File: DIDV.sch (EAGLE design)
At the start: 197 parts, among them IC1 PIC18F4550_TQFP

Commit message: -  Inclusão do circuito de buzzer; -  Correção e prevenção contra ruídos nas linhas comunicação;
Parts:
- removed C1, C2: (no value), rcl:C-EUC0805
- removed D1: BAS40, diode:BAS40
- removed JP1: (no value), jumper:JP1Q
- removed Q1: (no value), crystal:CRYSTALHC49UP
- removed R1, R2: (no value), rcl:R-EU_R0603
- added C30, C31, C32, C33, C34, C35, C36, C37, C38, C39, C40, C41, C42, C43, C44, C46: (no value), rcl:C-EUC0603K
- added C45: (no value), rcl:C-USC0805K
- added D5: BAS40, diode:BAS40
- added D6: BAS21, diode:BAS40
- added JP4: (no value), jumper:JP2E
- added LSP1: LSP10, solpad:LSP10
- added Q3: (no value), crystal:CRYSTALHC49U-V
- added Q4: BC817, transistor-npn:BC817-16LT1SMD
- added R105, R106, R107, R108, R109, R110, R111, R112, R113: (no value), rcl:R-EU_R0603
- added SG2: F/CM12P, buzzer:F/CM12P
- added SJ6: JUMPER-PAD-3-2OF3_NC_BY_PASTE, SparkFun-Passives:JUMPER-PAD-3-2OF3_NC_BY_PASTE
- C15, C16, C4: device rcl:C-EUC0603K -> rcl:C-EUC0805
- C3: device rcl:CPOL-EU140CLH-1014 -> rcl:C-EUC0805
- C5: device rcl:C-EUC0805 -> rcl:CPOL-EU140CLH-1014
- C6: device rcl:C-EUC0805 -> rcl:C-EUC0603K
- D2: value (none) -> BAS40; device diode:DIODE-SMC -> diode:BAS40
- D3: value BAS70 -> (none); device diode:BAS70 -> diode:DIODE-SMC
- D4: value BAS40 -> BAS70; device diode:BAS40 -> diode:BAS70
- JP2: device jumper:JP1E -> jumper:JP1Q
- JP3: device jumper:JP2E -> jumper:JP1E
- Q2: device crystal:CRYSTALHC49U-V -> crystal:CRYSTALHC49UP
- R5, R6: device rcl:R-US_R0805 -> rcl:R-EU_R0603
- R77, R78: device rcl:R-EU_R0603 -> rcl:R-US_R0805
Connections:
- removed net N$3: R81.2, S3.1, S3.2
- removed net N$43: IC1.RA2/AN2/VREF-/CVREF
- removed net N$9: C5.1, C6.1, D4.C, L1.1
- new net BUZZER: IC1.RB3/AN9/CCP2/VPO, SJ6.1
- new net N$10: C34.2, IC4.SIN, R109.2
- new net N$12: C35.2, IC5.SIN, R110.2
- new net N$13: IC5.SOUT, R111.1
- new net N$17: LSP1.MP, SJ6.3
- new net N$2: C7.1, C8.1, D5.C, L1.1
- new net N$23: C45.2, D6.A, Q4.C, SG2.1
- new net N$24: R112.1, SJ6.2
- new net N$25: C46.1, Q4.B, R112.2, R113.2
- new net N$5: R85.2, S3.1, S3.2
- new net N$6: C32.2, IC2.SIN, R107.2
- new net N$7: C33.2, IC3.SIN, R108.2
- net AGND: now also C3.2, C30.2, C31.2, C32.1, C33.1, C34.1, C35.1, C36.2, C37.2, C38.2, C39.2, C40.2, C41.2, C42.2, C43.2, C44.1, C46.2, C5.-, D4.A, JP2.1, JP4.1, Q4.E, R105.1, R113.1, R23.1, R3.1, R40.1, R57.1, R97.1, R98.1; no longer C1.2, C2.2, C3.-, C5.2, D3.A, JP1.1, JP3.1, R1.1, R103.1, R21.1, R38.1, R55.1, R72.1, R73.1
- net B00: now also C19.1; no longer C17.1
- net B01: now also C20.1; no longer C18.1
- net B02: now also C21.1; no longer C19.1
- net B03: now also C22.1; no longer C20.1
- net B04: now also C23.1; no longer C21.1
- net B05: now also C30.1; no longer C28.1
- net BACKSPACE: now also C25.1, R100.1; no longer C23.1, R98.1
- net D+: now also R6.1; no longer R4.1
- net D-: now also R5.1; no longer R3.1
- net DOWN: now also C31.1, R106.1; no longer C29.1, R104.1
- net ENTER: now also C24.1, R99.1; no longer C22.1, R97.1
- net ESC: now also C26.1, R101.1; no longer C24.1, R99.1
- net ESPAÇO: now also C27.1, R102.1; no longer C25.1, R100.1
- net FIM: now also C28.1, IC1.RA2/AN2/VREF-/CVREF, R103.1; no longer C26.1, IC1.RB3/AN9/CCP2/VPO, R101.1
- net GSCLK: now also C36.1, C37.1, C38.1, C39.1
- net M00: now also R58.1; no longer R56.1
- net M01: now also R59.1; no longer R57.1
- net M02: now also R60.1; no longer R58.1
- net M03: now also R61.1; no longer R59.1
- net M04: now also R62.1; no longer R60.1
- net M05: now also R63.1; no longer R61.1
- net M06: now also R64.1; no longer R62.1
- net M07: now also R65.1; no longer R63.1
- net M08: now also R66.1; no longer R64.1
- net M09: now also R67.1; no longer R65.1
- net M10: now also R68.1; no longer R66.1
- net M11: now also R69.1; no longer R67.1
- net M12: now also R70.1; no longer R68.1
- net M13: now also R71.1; no longer R69.1
- net M14: now also R72.1; no longer R70.1
- net M15: now also R73.1; no longer R71.1
- net M16: now also R7.1; no longer R5.1
- net M17: now also R8.1; no longer R6.1
- net M18: now also R9.1; no longer R7.1
- net M19: now also R10.1; no longer R8.1
- net M20: now also R11.1; no longer R9.1
- net M21: now also R12.1; no longer R10.1
- net M22: now also R13.1; no longer R11.1
- net M23: now also R14.1; no longer R12.1
- net M24: now also R15.1; no longer R13.1
- net M25: now also R16.1; no longer R14.1
- net M26: now also R17.1; no longer R15.1
- net M27: now also R18.1; no longer R16.1
- net M28: now also R19.1; no longer R17.1
- net M29: now also R20.1; no longer R18.1
- net M30: now also R21.1; no longer R19.1
- net M31: now also R22.1; no longer R20.1
- net M32: now also R41.1; no longer R39.1
- net M33: now also R42.1; no longer R40.1
- net M34: now also R43.1; no longer R41.1
- net M35: now also R44.1; no longer R42.1
- net M36: now also R45.1; no longer R43.1
- net M37: now also R46.1; no longer R44.1
- net M38: now also R47.1; no longer R45.1
- net M39: now also R48.1; no longer R46.1
- net M40: now also R49.1; no longer R47.1
- net M41: now also R50.1; no longer R48.1
- net M42: now also R51.1; no longer R49.1
- net M43: now also R52.1; no longer R50.1
- net M44: now also R53.1; no longer R51.1
- net M45: now also R54.1; no longer R52.1
- net M46: now also R55.1; no longer R53.1
- net M47: now also R56.1; no longer R54.1
- net M48: now also R24.1; no longer R22.1
- net M49: now also R25.1; no longer R23.1
- net M50: now also R26.1; no longer R24.1
- net M51: now also R27.1; no longer R25.1
- net M52: now also R28.1; no longer R26.1
- net M53: now also R29.1; no longer R27.1
- net M54: now also R30.1; no longer R28.1
- net M55: now also R31.1; no longer R29.1
- net M56: now also R32.1; no longer R30.1
- net M57: now also R33.1; no longer R31.1
- net M58: now also R34.1; no longer R32.1
- net M59: now also R35.1; no longer R33.1
- net M60: now also R36.1; no longer R34.1
- net M61: now also R37.1; no longer R35.1
- net M62: now also R38.1; no longer R36.1
- net M63: now also R39.1; no longer R37.1
- net MCLR: now also JP3.1; no longer JP2.1
- net N$109: now also D3.A, JP2.2; no longer D2.A, JP1.2
- net N$110: now also R3.2; no longer R1.2
- net N$111: now also C6.1, D2.C; no longer C4.1, D1.C
- net N$112: now also D2.A, R4.1; no longer D1.A, R2.1
- net N$113: now also C3.1, C4.1, C5.+, D4.C; no longer C1.1, C2.1, C3.+, D2.C
- net N$114: now also D5.A; no longer D4.A
- net N$115: now also R6.2; no longer R4.2
- net N$116: now also R5.2; no longer R3.2
- net N$118: now also R57.2, R77.2; no longer R55.2, R75.2
- net N$14: now also R79.2; no longer R77.2
- net N$144: now also R74.2, R75.2; no longer R72.2, R73.2
- net N$31: now also R82.2; no longer R80.2
- net N$38: now also R81.2; no longer R79.2
- net N$39: now also R80.2; no longer R78.2
- net N$64: now also R23.2, R76.2; no longer R21.2, R74.2
- net N$68: now also R98.2; no longer R88.2
- net N$69: now also R97.2; no longer R87.2
- net N$70: now also R88.2; no longer R86.2
- net N$71: now also R87.2; no longer R85.2
- net N$72: now also R86.2; no longer R82.2
- net N$8: now also R105.2; no longer R103.2
- net N$85: now also R40.2, R78.2; no longer R38.2, R76.2
- net OSC1: now also C17.1, Q3.1; no longer C15.1, Q1.1
- net OSC2: now also C18.1, Q3.2; no longer C16.1, Q1.2
- net PGC_OUT: now also JP4.3; no longer JP3.3
- net PGD_OUT: now also JP4.2; no longer JP3.2
- net SCLK: now also C40.1, C41.1, C42.1, C43.1
- net SIN: now also R107.1; no longer IC2.SIN
- net SO2: now also R108.1; no longer IC3.SIN
- net SO3: now also R109.1; no longer IC4.SIN
- net SO4: now also R110.1; no longer IC5.SIN
- net SOUT: now also C44.2, R111.2; no longer IC5.SOUT
- net UP: now also C29.1, R104.1; no longer C27.1, R102.1
- net VCC: now also C15.1, C16.1, C45.1, D6.C, JP3.2, R103.2, R106.2, R21.2, R38.2, R4.2, R55.2, R72.2, R73.2, SG2.2; no longer C10.1, C9.1, JP2.2, R2.2, R23.2, R40.2, R5.2, R57.2, R6.2, R97.2, R98.2
- net VUSB: now also C10.1, C9.1; no longer C7.1, C8.1
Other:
- note added: "On Raspberry Pi B+"
- moved on the sheet: C10, C11, C12, C13, C14, C15, C16, C17, C18, C19, C20, C21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

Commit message: Rev4 - Adição do circuito de Alta Latência - Previsão de conexão de módulos de expansão - Correção de falhas e previsão de melhorias com relação a estabilidade do sistema - Definição dos valores iniciais para cada componente - Previsão de circuito conversor de nivel para possivel feature implementável de atualização de firmware.
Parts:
- removed C10, C11, C12, C13, C14, C15, C16, C3, C4, C7, C8, C9: (no value), rcl:C-EUC0805
- removed C17, C18, C19, C20, C21, C22, C23, C24, C25, C31, C6: (no value), rcl:C-EUC0603K
- removed C5: (no value), rcl:CPOL-EU140CLH-1014
- removed D2, D5: BAS40, diode:BAS40
- removed D3: (no value), diode:DIODE-SMC
- removed JP2: (no value), jumper:JP1Q
- removed JP3: (no value), jumper:JP1E
- removed JP4: (no value), jumper:JP2E
- removed L1: (no value), inductor-neosid:MS50
- removed LSP1: LSP10, solpad:LSP10
- removed Q2: (no value), crystal:CRYSTALHC49UP
- removed Q3: (no value), crystal:CRYSTALHC49U-V
- removed Q4: BC817, transistor-npn:BC817-16LT1SMD
- removed R10, R11, R12, R13, R14, R15, R16, R17, R18, R19, R20, R21, R22, R23, R24, R25, R26, R27, R28, R29, R30, R31, R32, R33, R34, R35, R36, R37, R38, R39, R40, R41, R42, R43, R44, R49, R7, R8, R9: (no value), rcl:R-US_R0805
- removed R3, R4, R5, R6: (no value), rcl:R-EU_R0603
- removed S1, S10, S11, S12, S13, S2, S3, S4, S5, S6, S7, S8, S9: (no value), SparkFun-Electromechanical:TAC_SWITCHSMD
- removed SG2: F/CM12P, buzzer:F/CM12P
- removed SJ6: JUMPER-PAD-3-2OF3_NC_BY_PASTE, SparkFun-Passives:JUMPER-PAD-3-2OF3_NC_BY_PASTE
- added C47, C56: 10nf/50V, rcl:C-EUC0603K
- added C48, C49, C50, C51, C52, C53, C54, C55: 100nf/50V, rcl:C-EUC0805
- added D7, D8: BAS21, diode:BAS40
- added JP75, JP86: (no value), jumper:JP1Q
- added JP83: (no value), jumper:JP2E
- added JP84: (no value), jumper:JP1E
- added JP85: (no value), jumper:JP7Q
- added K1: 4052, relay:4052
- added L3: 330m, inductor-neosid:MS50
- added Q10: BC817, transistor-npn:BC817-16LT1SMD
- added R114, R115, R116, R117, R118, R119, R120, R122, R124: (no value), rcl:R-US_R0805
- added R121, R123: 649, rcl:R-US_R0805
- added R125: 22, rcl:R-EU_R0603
- added R126: 10k, rcl:R-EU_R0603
- added R127, R128: 100, rcl:R-EU_R0603
- added R129: 100k, rcl:R-US_R0805
- added R130: 0r, rcl:R-EU_R0603
- added R131: 150k, rcl:R-EU_R0603
- added R132: 100k, rcl:R-EU_R0603
- added XT1: 20Mhz, crystal:CRYSTALHC49UP
- added XT2: (no value), crystal:CRYSTALHC49U-V
- added Z2: 5v1, diode:BAS70
- C26: value (none) -> 470uf/35V; device rcl:C-EUC0603K -> rcl:CPOL-EU140CLH-1014
- C27, C28, C32, C33: value (none) -> 100nf/50V; device rcl:C-EUC0603K -> rcl:C-EUC0805
- C29, C30, C36, C37, C38, C39, C40, C41, C42, C43, C44, C46: value (none) -> 100nf/50V
- C34, C35: value (none) -> 22pf/50V
- C45: value (none) -> 100nf/50V; device rcl:C-USC0805K -> rcl:C-EUC0603K
- D4: value BAS70 -> S3J; device diode:BAS70 -> diode:DIODE-SMC
- IC1: value PIC18F4550_TQFP -> (none); device microchip:PIC18F4550_TQFP -> TLC5940:IC-PACKAGE_DIL28-3
- IC5: value (none) -> PIC18F4550; device TLC5940:IC-PACKAGE_DIL28-3 -> microchip:PIC18F4550_TQFP
- L2: value (none) -> 330m
- R100, R102, R103, R104, R105, R106, R107, R108, R109, R110, R111, R112, R113, R79, R80, R81, R83, R85, R87, R88, R89, R90, R91, R92, R93, R94, R95, R96, R97, R98: device rcl:R-EU_R0603 -> rcl:R-US_R0805
- R101, R99: value (none) -> 22
- R58, R60, R70, R77: value (none) -> 22; device rcl:R-US_R0805 -> rcl:R-EU_R0603
- R82, R84: value (none) -> 649; device rcl:R-EU_R0603 -> rcl:R-US_R0805
- R86: value (none) -> 1M
- SJ1: value JUMPER-PAD-2-NOYES_SILK -> JUMPER-PAD-3-2OF3_NC_BY_PASTE; device SparkFun-Passives:JUMPER-PAD-2-NOYES_SILK -> SparkFun-Passives:JUMPER-PAD-3-2OF3_NC_BY_PASTE
- SJ3: value JUMPER-PAD-3-2OF3_NC_BY_PASTE -> JUMPER-PAD-2-NOYES_SILK; device SparkFun-Passives:JUMPER-PAD-3-2OF3_NC_BY_PASTE -> SparkFun-Passives:JUMPER-PAD-2-NOYES_SILK
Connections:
- removed net B00: C19.1, IC1.RD0/SPP0, R91.1, S9.3, S9.4
- removed net B01: C20.1, IC1.RD1/SPP1, R92.1, S10.3, S10.4
- removed net B02: C21.1, IC1.RD2/SPP2, R93.1, S11.3, S11.4
- removed net B03: C22.1, IC1.RD3/SPP3, R94.1, S12.3, S12.4
- removed net B04: C23.1, IC1.RD4/SPP4, R95.1, S8.3, S8.4
- removed net B05: C30.1, IC1.RD5/SPP5/P1B, R96.1, S7.3, S7.4
- removed net BACKSPACE: C25.1, IC1.RC1/T1OSI/ICCP2/!UOE, R100.1, S4.3, S4.4
- removed net BUZZER: IC1.RB3/AN9/CCP2/VPO, SJ6.1
- removed net DOWN: C31.1, IC1.RD7/SPP7/P1D, R106.1, S14.3, S14.4
- removed net ENTER: C24.1, IC1.RC0/TIOSO/T13CKI, R99.1, S3.3, S3.4
- removed net ESC: C26.1, IC1.RB2/AN8/INT2/VMO, R101.1, S5.3, S5.4
- removed net ESPAÇO: C27.1, IC1.RC6/TX/CK, R102.1, S6.3, S6.4
- removed net FIM: C28.1, IC1.RA2/AN2/VREF-/CVREF, R103.1, S2.3, S2.4
- removed net N$10: C34.2, IC4.SIN, R109.2
- removed net N$109: D3.A, JP2.2
- removed net N$110: R3.2, S13.1, S13.2
- removed net N$111: C6.1, D2.C, R89.2, S13.3, S13.4
- removed net N$112: D2.A, R4.1
- removed net N$113: C3.1, C4.1, C5.+, D3.C, D4.C, L2.1
- removed net N$114: D5.A, U1.VBUS
- removed net N$115: R6.2, U1.D+
- removed net N$116: R5.2, U1.D-
- removed net N$118: IC4.IREF, R57.2, R77.2
- removed net N$12: C35.2, IC5.SIN, R110.2
- removed net N$13: IC5.SOUT, R111.1
- removed net N$14: R79.2, S9.1, S9.2
- removed net N$144: IC2.IREF, R74.2, R75.2
- removed net N$17: LSP1.MP, SJ6.3
- removed net N$18: IC1.RE2/AN7/OESPP
- removed net N$19: IC1.RE1/AN6/CK2SPP
- removed net N$2: C7.1, C8.1, D5.C, L1.1
- removed net N$20: IC1.RE0/AN5/CK1SPP
- removed net N$21: IC1.RA5/AN4/!SS!/HLVDIN/C2OUT
- removed net N$22: IC1.RA4/T0CKI/CIOUT/RCV
- removed net N$23: C45.2, D6.A, Q4.C, SG2.1
- removed net N$24: R112.1, SJ6.2
- removed net N$25: C46.1, Q4.B, R112.2, R113.2
- removed net N$29: R84.2, S7.1, S7.2
- removed net N$30: R83.2, S8.1, S8.2
- removed net N$31: R82.2, S12.1, S12.2
- removed net N$36: IC1.RB4/AN11/KBI0/CSSPP
- removed net N$37: IC1.RB5/KBI1/PGM
- removed net N$38: R81.2, S11.1, S11.2
- removed net N$39: R80.2, S10.1, S10.2
- removed net N$44: IC1.RA3/AN3/VREF+
- removed net N$5: R85.2, S3.1, S3.2
- removed net N$6: C32.2, IC2.SIN, R107.2
- removed net N$64: IC3.IREF, R23.2, R76.2
- removed net N$68: R98.2, S1.1, S1.2
- removed net N$69: R97.2, S2.1, S2.2
- removed net N$7: C33.2, IC3.SIN, R108.2
- removed net N$70: R88.2, S6.1, S6.2
- removed net N$71: R87.2, S5.1, S5.2
- removed net N$72: R86.2, S4.1, S4.2
- removed net N$8: R105.2, S14.1, S14.2
- removed net N$85: IC5.IREF, R40.2, R78.2
- removed net UP: C29.1, IC1.RD6/SPP6/P1C, R104.1, S1.3, S1.4
- new net EXP: IC5.RD4/SPP4, R131.2
- new net EXPA: JP85.4, K12.S
- new net EXPB: JP85.3, K13.P
- new net N$126: IC5.RE2/AN7/OESPP
- new net N$127: IC5.RE1/AN6/CK2SPP
- new net N$128: IC5.RE0/AN5/CK1SPP
- new net N$129: IC5.RA5/AN4/!SS!/HLVDIN/C2OUT
- new net N$130: IC5.RA4/T0CKI/CIOUT/RCV
- new net N$131: IC5.RB4/AN11/KBI0/CSSPP
- new net N$132: IC5.RB5/KBI1/PGM
- new net N$133: IC5.RA3/AN3/VREF+
- new net N$134: R127.2, S14.1, S14.2
- new net N$135: C47.1, D7.C, R128.2, S14.3, S14.4
- new net N$136: D7.A, R126.1
- new net N$137: D4.A, JP75.2
- new net N$138: C26.+, C27.1, C28.1, D4.C, L2.1, Z2.C
- new net N$139: R70.2, U1.D+
- new net N$140: R77.2, U1.D-
- new net N$141: D6.A, U1.VBUS
- new net N$142: IC1.IREF, R82.2, R83.2
- new net N$143: IC3.IREF, R121.2, R122.2
- new net N$145: IC4.IREF, R123.2, R124.2
- new net N$146: IC2.IREF, R84.2, R85.2
- new net N$147: C32.1, C33.1, D6.C, L3.1
- new net N$148: C30.2, IC2.SIN, R60.2
- new net N$149: C29.2, IC1.SIN, R58.2
- new net N$150: C37.2, IC4.SIN, R101.2
- new net N$151: C36.2, IC3.SIN, R99.2
- new net N$152: IC3.SOUT, R125.1
- new net N$153: IC5.RC1/T1OSI/ICCP2/!UOE
- new net N$154: IC5.RD0/SPP0
- new net N$155: IC5.RD1/SPP1
- new net N$156: IC5.RD2/SPP2
- new net N$157: IC5.RD3/SPP3
- new net N$158: IC5.RC6/TX/CK
- new net N$159: IC5.RC0/TIOSO/T13CKI
- new net N$160: IC5.RA2/AN2/VREF-/CVREF
- new net N$161: IC5.!MCLR!/VPP/RE3
- new net N$162: IC5.RB2/AN8/INT2/VMO
- new net N$163: IC5.RB3/AN9/CCP2/VPO
- new net N$164: IC5.RD7/SPP7/P1D
- new net N$165: IC5.RD6/SPP6/P1C
- new net N$166: Q10.C, R130.1
- new net N$167: C56.1, Q10.B, R131.1, R132.2
- new net N$168: D8.A, K11.2, R130.2
- new net N$169: K13.O
- new net RA: IC5.RD5/SPP5/P1B, JP85.2, JP86.2, R129.1
- new net RB: JP85.1, JP86.1
- new net SOUT_: IC5.RB0/AN12/INT0/LFT0/SDI/SDA, K12.O, K13.S
- net AGND: now also C26.-, C29.1, C30.1, C32.2, C33.2, C34.2, C35.2, C36.1, C37.1, C38.1, C44.2, C45.2, C47.2, C48.2, C49.2, C50.2, C51.2, C52.2, C53.2, C54.2, C55.2, C56.2, IC1.GND, IC5.VSS, IC5.VSS@1, JP75.1, JP83.1, JP85.11, JP85.13, Q10.E, R121.1, R122.1, R123.1, R124.1, R127.1, R132.1, Z2.A; no longer C10.2, C11.2, C12.2, C13.2, C14.2, C15.2, C16.2, C17.2, C18.2, C19.2, C20.2, C21.2, C22.2, C23.2, C24.2, C25.2, C26.2, C29.2, C3.2, C30.2, C31.2, C32.1, C33.1, C34.1, C35.1, C36.2, C37.2, C38.2, C4.2, C44.1, C5.-, C6.2, C7.2, C8.2, C9.2, D4.A, IC1.VSS, IC1.VSS@1, IC5.GND, JP2.1, JP4.1, Q4.E, R105.1, R113.1, R23.1, R3.1, R40.1, R57.1, R74.1, R75.1, R76.1, R77.1, R78.1, R79.1, R80.1, R81.1, R86.1, R87.1, R88.1, R97.1, R98.1
- net BLANK: now also IC1.BLANK, IC5.RA1/AN1, JP85.7, TP21.1, TP22.1, TP7.1, TP8.1; no longer IC1.RA1/AN1, IC5.BLANK, TP11.1, TP18.1, TP25.1, TP4.1
- net D+: now also R70.1, SJ2.3; no longer R6.1, SJ4.3
- net D+_: now also IC5.RC5/D+/VP, SJ2.2; no longer IC1.RC5/D+/VP, SJ4.2
- net D-: now also R77.1, SJ1.3; no longer R5.1, SJ5.3
- net D-_: now also IC5.RC4/D-/VM, SJ1.2; no longer IC1.RC4/D-/VM, SJ5.2
- net GSCLK: now also C43.1, C44.1, C45.1, C46.1, IC1.GSCLK, IC5.RC2/CCP1/P1A, JP85.5, TP11.1, TP12.1, TP25.1, TP26.1; no longer C36.1, C37.1, C38.1, C39.1, IC1.RC2/CCP1/P1A, IC5.GSCLK, TP13.1, TP20.1, TP27.1, TP6.1
- net M00: now also R46.1; no longer R58.1
- net M01: now also R48.1; no longer R59.1
- net M02: now also R51.1; no longer R60.1
- net M03: now also R53.1; no longer R61.1
- net M04: now also R55.1; no longer R62.1
- net M05: now also R57.1; no longer R63.1
- net M06: now also R61.1; no longer R64.1
- net M07: now also R63.1; no longer R65.1
- net M08: now also R65.1; no longer R66.1
- net M10: now also R69.1; no longer R68.1
- net M11: now also R72.1; no longer R69.1
- net M12: now also R74.1; no longer R70.1
- net M13: now also R76.1; no longer R71.1
- net M14: now also R79.1; no longer R72.1
- net M15: now also R81.1; no longer R73.1
- net M16: now also IC1.OUT0, R45.1; no longer IC3.OUT0, R7.1
- net M17: now also IC1.OUT1, R47.1; no longer IC3.OUT1, R8.1
- net M18: now also IC1.OUT2, R50.1; no longer IC3.OUT2, R9.1
- net M19: now also IC1.OUT3, R52.1; no longer IC3.OUT3, R10.1
- net M20: now also IC1.OUT4, R54.1; no longer IC3.OUT4, R11.1
- net M21: now also IC1.OUT5, R56.1; no longer IC3.OUT5, R12.1
- net M22: now also IC1.OUT6, R59.1; no longer IC3.OUT6, R13.1
- net M23: now also IC1.OUT7, R62.1; no longer IC3.OUT7, R14.1
- net M24: now also IC1.OUT8, R64.1; no longer IC3.OUT8, R15.1
- net M25: now also IC1.OUT9, R66.1; no longer IC3.OUT9, R16.1
- net M26: now also IC1.OUT10, R68.1; no longer IC3.OUT10, R17.1
- net M27: now also IC1.OUT11, R71.1; no longer IC3.OUT11, R18.1
- net M28: now also IC1.OUT12, R73.1; no longer IC3.OUT12, R19.1
- net M29: now also IC1.OUT13, R75.1; no longer IC3.OUT13, R20.1
- net M30: now also IC1.OUT14, R78.1; no longer IC3.OUT14, R21.1
- net M31: now also IC1.OUT15, R80.1; no longer IC3.OUT15, R22.1
- net M32: now also R88.1; no longer R41.1
- net M33: now also R90.1; no longer R42.1
- net M34: now also R92.1; no longer R43.1
- net M35: now also R94.1; no longer R44.1
- net M36: now also R96.1; no longer R45.1
- net M37: now also R98.1; no longer R46.1
- net M38: now also R102.1; no longer R47.1
- net M39: now also R104.1; no longer R48.1
- net M40: now also R106.1; no longer R49.1
- net M41: now also R108.1; no longer R50.1
- net M42: now also R110.1; no longer R51.1
- net M43: now also R112.1; no longer R52.1
- net M44: now also R114.1; no longer R53.1
- net M45: now also R116.1; no longer R54.1
- net M46: now also R118.1; no longer R55.1
- net M47: now also R120.1; no longer R56.1
- net M48: now also IC3.OUT0, R87.1; no longer IC5.OUT0, R24.1
- net M49: now also IC3.OUT1, R89.1; no longer IC5.OUT1, R25.1
- net M50: now also IC3.OUT2, R91.1; no longer IC5.OUT2, R26.1
- net M51: now also IC3.OUT3, R93.1; no longer IC5.OUT3, R27.1
- net M52: now also IC3.OUT4, R95.1; no longer IC5.OUT4, R28.1
- net M53: now also IC3.OUT5, R97.1; no longer IC5.OUT5, R29.1
- net M54: now also IC3.OUT6, R100.1; no longer IC5.OUT6, R30.1
- net M55: now also IC3.OUT7, R103.1; no longer IC5.OUT7, R31.1
- net M56: now also IC3.OUT8, R105.1; no longer IC5.OUT8, R32.1
- net M57: now also IC3.OUT9, R107.1; no longer IC5.OUT9, R33.1
- net M58: now also IC3.OUT10, R109.1; no longer IC5.OUT10, R34.1
- net M59: now also IC3.OUT11, R111.1; no longer IC5.OUT11, R35.1
- net M60: now also IC3.OUT12, R113.1; no longer IC5.OUT12, R36.1
- net M61: now also IC3.OUT13, R115.1; no longer IC5.OUT13, R37.1
- net M62: now also IC3.OUT14, R117.1; no longer IC5.OUT14, R38.1
- net M63: now also IC3.OUT15, R119.1; no longer IC5.OUT15, R39.1
- net MCLR: now also JP84.1, SJ3.1; no longer JP3.1, SJ1.1
- net NC: now also IC1.XERR; no longer IC5.XERR
- net OSC1: now also C34.1, IC5.OSC1/CLKI, R86.2, XT1.1, XT2.1; no longer C17.1, IC1.OSC1/CLKI, Q2.1, Q3.1, R90.2
- net OSC2: now also C35.1, IC5.RA6/OSC2/CLKO, R86.1, XT1.2, XT2.2; no longer C18.1, IC1.RA6/OSC2/CLKO, Q2.2, Q3.2, R90.1
- net PGC: now also IC5.RB6/KBI2/PGC, SJ4.2; no longer IC1.RB6/KBI2/PGC, SJ2.2
- net PGC_OUT: now also JP83.3, SJ4.3; no longer JP4.3, SJ2.3
- net PGD: now also IC5.RB7/BKI3/PGD, SJ5.2; no longer IC1.RB7/BKI3/PGD, SJ3.2
- net PGD_OUT: now also JP83.2, SJ5.3; no longer JP4.2, SJ3.3
- net RB6: now also SJ4.1; no longer SJ2.1
- net RB7: now also SJ5.1; no longer SJ3.1
- net RC4: now also SJ1.1; no longer SJ5.1
- net RC5: now also SJ2.1; no longer SJ4.1
- net RESET: now also R128.1, SJ3.2; no longer IC1.!MCLR!/VPP/RE3, R89.1, SJ1.2
- net SCLK: now also C39.1, IC1.SCLK, IC5.RB1/AN10/INT1/SCK/SCL, JP85.6, TP17.1, TP18.1, TP3.1, TP4.1; no longer C43.1, IC1.RB1/AN10/INT1/SCK/SCL, IC5.SCLK, TP16.1, TP2.1, TP23.1, TP9.1
- net SIN: now also IC5.RC7/RX/DT/SDO, R60.1, TP2.1; no longer IC1.RC7/RX/DT/SDO, R107.1, TP1.1
- net SO2: now also R58.1, TP1.1, TP14.1; no longer R108.1, TP7.1, TP8.1
- net SO3: now also IC1.SOUT, R101.1, TP13.1, TP16.1; no longer IC3.SOUT, R109.1, TP14.1, TP15.1
- net SO4: now also R99.1, TP15.1, TP27.1; no longer R110.1, TP21.1, TP22.1
- net SOUT: now also C38.2, K12.P, R125.2; no longer C44.2, IC1.RB0/AN12/INT0/LFT0/SDI/SDA, R111.2
- net VCC: now also C48.1, C49.1, C50.1, C51.1, C52.1, C53.1, D8.C, IC1.DCPRG, IC1.VCC, IC1.VPRG, IC5.VDD, IC5.VDD@1, JP84.2, JP85.12, JP85.14, K11.1, L3.2, R105.2, R107.2, R108.2, R109.2, R110.2, R111.2, R112.2, R113.2, R114.2, R115.2, R116.2, R117.2, R118.2, R119.2, R120.2, R126.2, R129.2, R57.2, R74.2, R75.2, R76.2, R78.2, R79.2, R80.2, R81.2, R87.2, R88.2, R89.2, R90.2, R97.2, R98.2, TP10.1, TP23.1, TP24.1, TP9.1; no longer C11.1, C12.1, C13.1, C14.1, C15.1, C16.1, C45.1, D6.C, IC1.VDD, IC1.VDD@1, IC5.DCPRG, IC5.VCC, IC5.VPRG, JP3.2, L1.2, R10.2, R101.2, R11.2, R12.2, R13.2, R14.2, R15.2, R16.2, R17.2, R18.2, R19.2, R20.2, R21.2, R22.2, R24.2, R25.2, R26.2, R27.2, R28.2, R29.2, R30.2, R31.2, R32.2, R33.2, R34.2, R35.2, R36.2, R37.2, R38.2, R39.2, R4.2, R41.2, R42.2, R43.2, R44.2, R49.2, R58.2, R60.2, R7.2, R70.2, R8.2, R9.2, R99.2, SG2.2, TP12.1, TP19.1, TP26.1, TP5.1
- net VUSB: now also C54.1, C55.1, IC5.VUSB; no longer C10.1, C9.1, IC1.VUSB
- net XLAT: now also IC1.XLAT, IC5.RA0/AN0, JP85.8, TP19.1, TP20.1, TP5.1, TP6.1; no longer IC1.RA0/AN0, IC5.XLAT, TP10.1, TP17.1, TP24.1, TP3.1
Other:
- note added: "16x10k"
- note added: "Previsto"
- note added: "Seletor_de_Expansão"
- note removed: "Botões"
- note removed: "On Raspberry Pi B+"
- moved on the sheet: C27, C28, C29, C30, C32, C33, C34, C35, C36, C37, C38, C39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

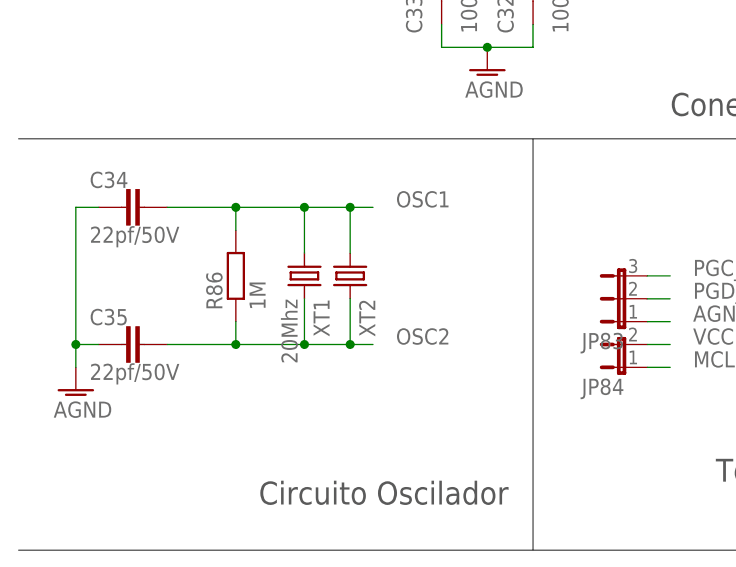
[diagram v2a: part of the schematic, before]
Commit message: Rev005
-  Inclusão de resistor série na linha do oscilador;
-  Nomenclatura correta dos componentes e nets;
-  Correção dos valores dos componentes.
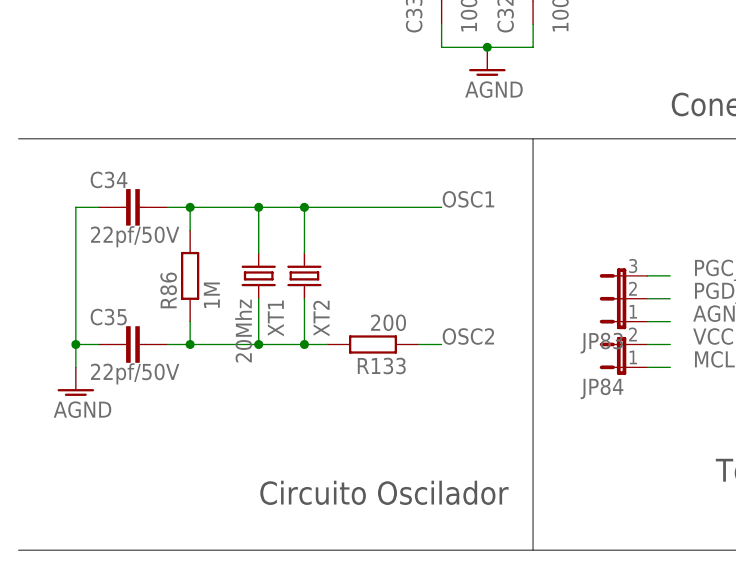
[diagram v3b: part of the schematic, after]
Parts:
- added R133: 200, rcl:R-EU_R0603
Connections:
- net OSC2: now also R133.1, R133.2
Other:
- moved on the sheet: R86, XT1, XT2
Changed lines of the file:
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@@
 <setting verticaltext="up"/>
 </settings>
-<grid distance="0.1" unitdist="inch" unit="inch" style="lines" multiple="1" display="no" altdistance="0.01" altunitdist="inch" altunit="inch"/>
+<grid distance="0.1" unitdist="inch" unit="inch" style="lines" multiple="1" display="yes" altdistance="0.01" altunitdist="inch" altunit="inch"/>
 <layers>
 <layer number="1" name="Top" color="4" fill="1" visible="no" active="no"/>
@@
 <part name="JP85" library="jumper" deviceset="JP7Q" device=""/>
 <part name="Q10" library="transistor-npn" deviceset="BC817*" device="SMD" technology="-16LT1" value="BC817"/>
+<part name="R133" library="rcl" deviceset="R-EU_" device="R0603" value="200"/>
 </parts>
 <sheets>
@@
 <instance part="C34" gate="G$1" x="50.8" y="215.9" rot="R270"/>
 <instance part="C35" gate="G$1" x="50.8" y="200.66" rot="R270"/>
-<instance part="R86" gate="G$1" x="60.96" y="208.28" rot="R90"/>
-<instance part="XT1" gate="G$1" x="68.58" y="208.28" rot="R270"/>
-<instance part="XT2" gate="G$1" x="73.66" y="208.28" rot="R270"/>
+<instance part="R86" gate="G$1" x="55.88" y="208.28" rot="R90"/>
+<instance part="XT1" gate="G$1" x="63.5" y="208.28" rot="R270"/>
+<instance part="XT2" gate="G$1" x="68.58" y="208.28" rot="R270"/>
 <instance part="AGND57" gate="VR1" x="43.18" y="195.58"/>
 <instance part="SJ4" gate="G$1" x="91.44" y="144.78" rot="R90"/>
@@
 <instance part="JP85" gate="B" x="416.56" y="73.66" rot="R90"/>
 <instance part="Q10" gate="G$1" x="304.8" y="58.42"/>
+<instance part="R133" gate="G$1" x="76.2" y="200.66" rot="R180"/>
 </instances>
 <busses>
@@
 <segment>
 <pinref part="C34" gate="G$1" pin="1"/>
-<wire x1="53.34" y1="215.9" x2="60.96" y2="215.9" width="0.1524" layer="91"/>
+<wire x1="53.34" y1="215.9" x2="55.88" y2="215.9" width="0.1524" layer="91"/>
 <pinref part="XT2" gate="G$1" pin="1"/>
-<wire x1="60.96" y1="215.9" x2="68.58" y2="215.9" width="0.1524" layer="91"/>
-<wire x1="68.58" y1="215.9" x2="73.66" y2="215.9" width="0.1524" layer="91"/>
-<wire x1="73.66" y1="215.9" x2="73.66" y2="210.82" width="0.1524" layer="91"/>
+<wire x1="55.88" y1="215.9" x2="63.5" y2="215.9" width="0.1524" layer="91"/>
+<wire x1="63.5" y1="215.9" x2="68.58" y2="215.9" width="0.1524" layer="91"/>
+<wire x1="68.58" y1="215.9" x2="68.58" y2="210.82" width="0.1524" layer="91"/>
 <pinref part="R86" gate="G$1" pin="2"/>
-<wire x1="60.96" y1="213.36" x2="60.96" y2="215.9" width="0.1524" layer="91"/>
-<junction x="60.96" y="215.9"/>
+<wire x1="55.88" y1="213.36" x2="55.88" y2="215.9" width="0.1524" layer="91"/>
+<junction x="55.88" y="215.9"/>
 <pinref part="XT1" gate="G$1" pin="1"/>
-<wire x1="68.58" y1="210.82" x2="68.58" y2="215.9" width="0.1524" layer="91"/>
+<wire x1="63.5" y1="210.82" x2="63.5" y2="215.9" width="0.1524" layer="91"/>
+<junction x="63.5" y="215.9"/>
+<wire x1="68.58" y1="215.9" x2="83.82" y2="215.9" width="0.1524" layer="91"/>
 <junction x="68.58" y="215.9"/>
-<wire x1="73.66" y1="215.9" x2="76.2" y2="215.9" width="0.1524" layer="91"/>
-<junction x="73.66" y="215.9"/>
-<label x="78.74" y="215.9" size="1.778" layer="95"/>
+<label x="83.82" y="215.9" size="1.778" layer="95"/>
 </segment>
 <segment>
@@
 <segment>
 <pinref part="XT2" gate="G$1" pin="2"/>
-<wire x1="73.66" y1="205.74" x2="73.66" y2="200.66" width="0.1524" layer="91"/>
+<wire x1="68.58" y1="205.74" x2="68.58" y2="200.66" width="0.1524" layer="91"/>
+<wire x1="68.58" y1="200.66" x2="63.5" y2="200.66" width="0.1524" layer="91"/>
+<pinref part="XT1" gate="G$1" pin="2"/>
+<wire x1="63.5" y1="205.74" x2="63.5" y2="200.66" width="0.1524" layer="91"/>
 <pinref part="C35" gate="G$1" pin="1"/>
-<wire x1="73.66" y1="200.66" x2="68.58" y2="200.66" width="0.1524" layer="91"/>
+<wire x1="53.34" y1="200.66" x2="55.88" y2="200.66" width="0.1524" layer="91"/>
+<junction x="63.5" y="200.66"/>
 <pinref part="R86" gate="G$1" pin="1"/>
-<wire x1="68.58" y1="200.66" x2="60.96" y2="200.66" width="0.1524" layer="91"/>
-<wire x1="60.96" y1="200.66" x2="53.34" y2="200.66" width="0.1524" layer="91"/>
-<wire x1="60.96" y1="203.2" x2="60.96" y2="200.66" width="0.1524" layer="91"/>
-<junction x="60.96" y="200.66"/>
-<pinref part="XT1" gate="G$1" pin="2"/>
-<wire x1="68.58" y1="205.74" x2="68.58" y2="200.66" width="0.1524" layer="91"/>
+<wire x1="55.88" y1="200.66" x2="63.5" y2="200.66" width="0.1524" layer="91"/>
+<wire x1="55.88" y1="203.2" x2="55.88" y2="200.66" width="0.1524" layer="91"/>
+<junction x="55.88" y="200.66"/>
+<pinref part="R133" gate="G$1" pin="2"/>
+<wire x1="71.12" y1="200.66" x2="68.58" y2="200.66" width="0.1524" layer="91"/>
 <junction x="68.58" y="200.66"/>
-<wire x1="73.66" y1="200.66" x2="76.2" y2="200.66" width="0.1524" layer="91"/>
-<junction x="73.66" y="200.66"/>
-<label x="78.74" y="200.66" size="1.778" layer="95"/>
 </segment>
 <segment>
@@
 <label x="241.3" y="66.04" size="1.778" layer="95"/>
 </segment>
-</net>
+<segment>
+<pinref part="R133" gate="G$1" pin="1"/>
+<wire x1="81.28" y1="200.66" x2="83.82" y2="200.66" width="0.1524" layer="91"/>
+<label x="83.82" y="200.66" size="1.778" layer="95"/>
+</segment>
+</net>
